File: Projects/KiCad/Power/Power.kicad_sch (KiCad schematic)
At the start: 46 parts, among them J1 Conn_01x02_Pin, J2 Conn_01x02_Pin, J3 Conn_01x02_Pin, J4 Conn_01x02_Pin, Q1 TJ8S06M3L, Q2 TJ8S06M3L, Q3 TJ8S06M3L, SW2 SW_SPDT, U1 NJM7812SDL1, U2 NJM7812SDL1, U3 NJM7812SDL1, U4 LTC4416EMS#PBF

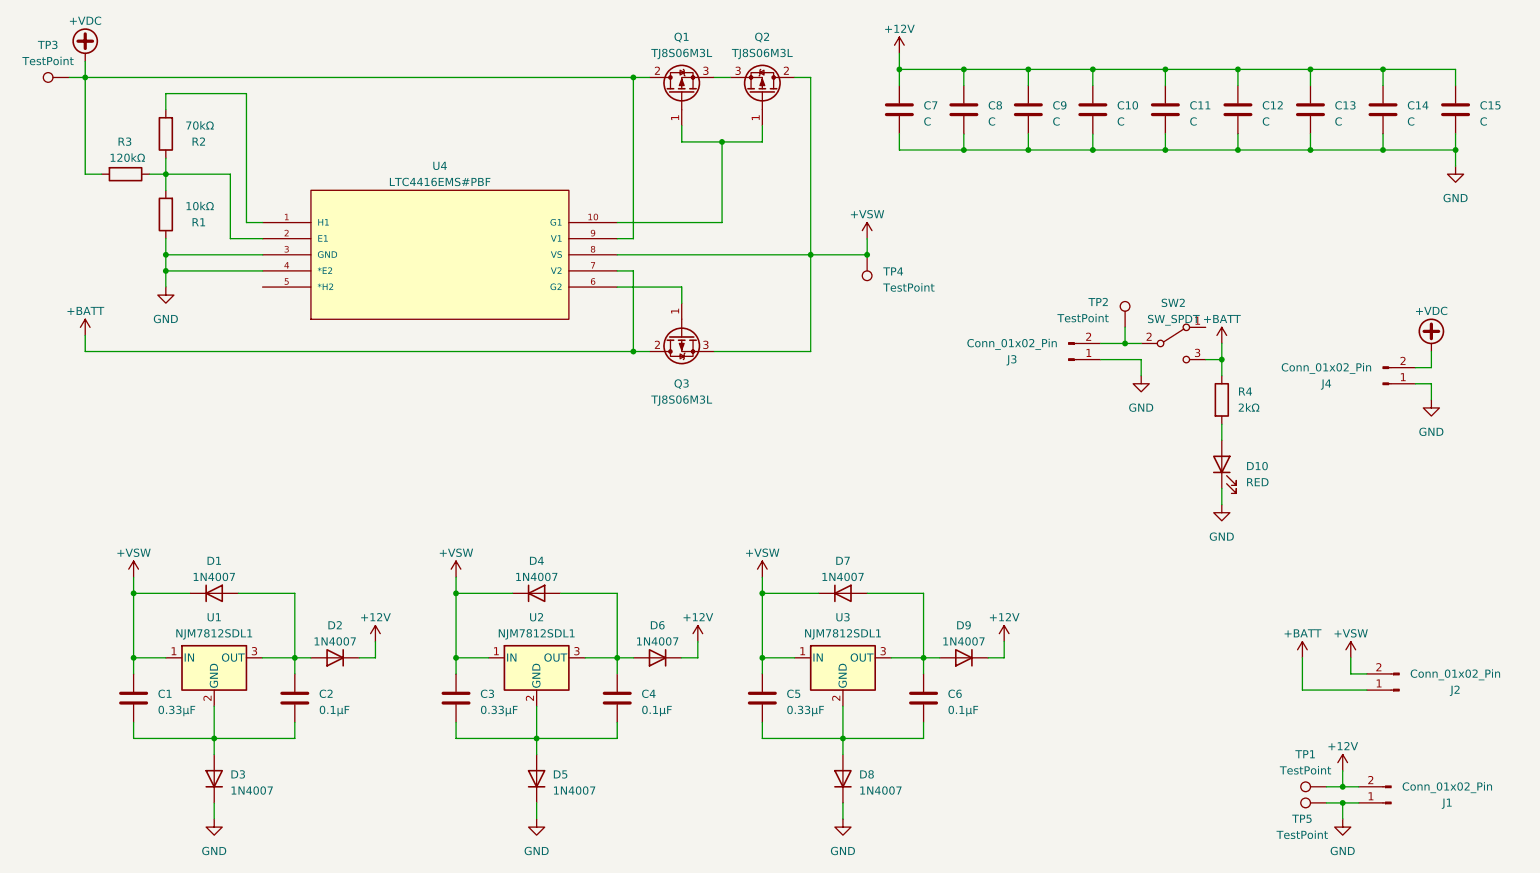
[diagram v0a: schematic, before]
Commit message: STEPファイルを再生成
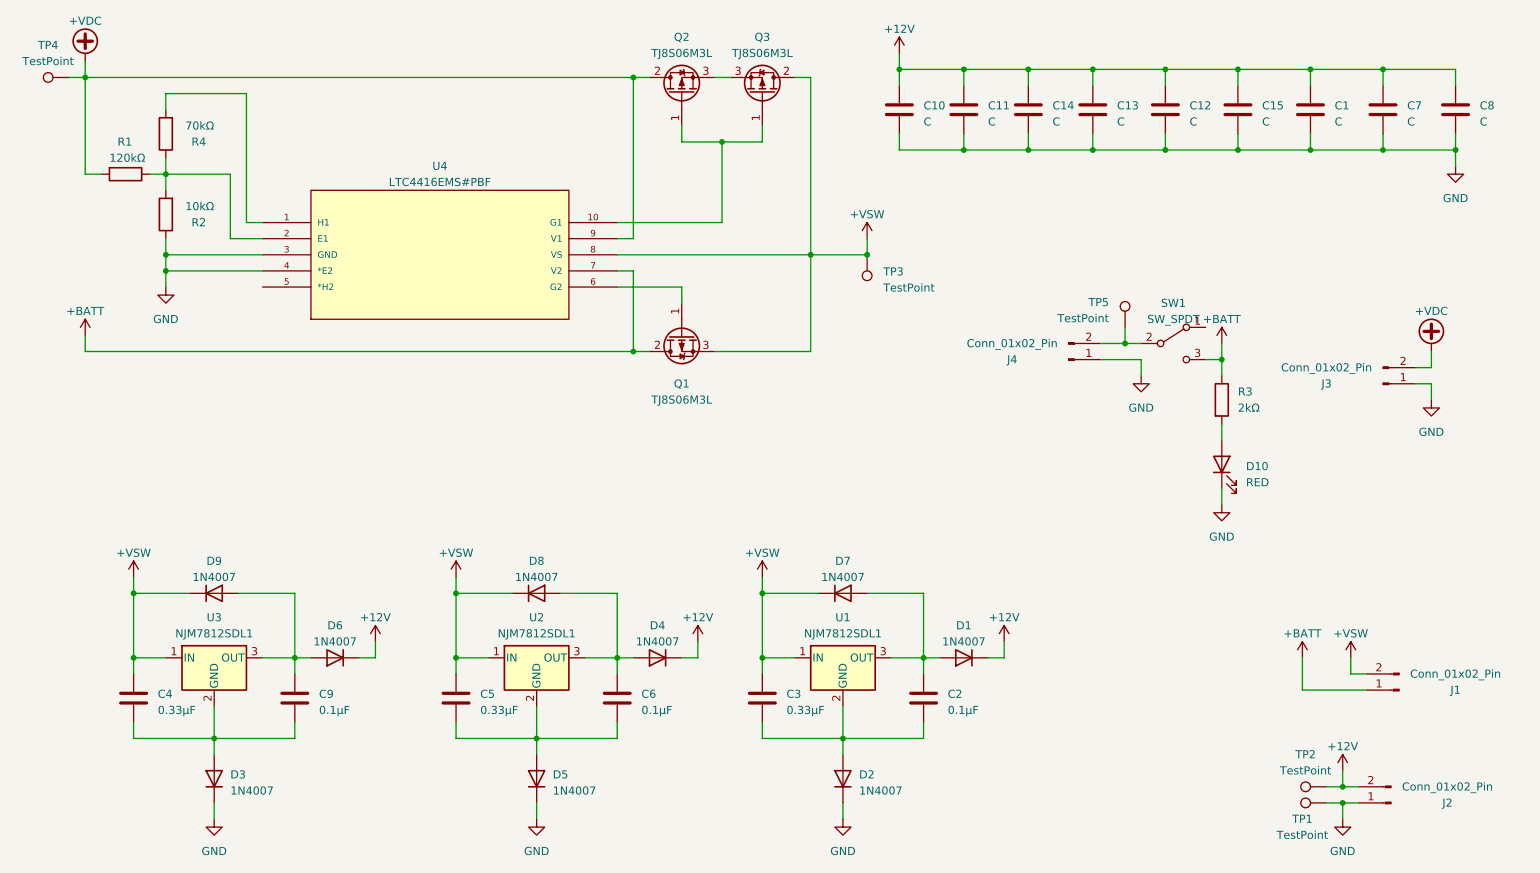
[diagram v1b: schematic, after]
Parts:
- renumbered C13 to C1, C7 to C10, C8 to C11, C11 to C12, C10 to C13, C9 to C14, C12 to C15, C6 to C2, C5 to C3, C1 to C4, C3 to C5, C4 to C6, C14 to C7, C15 to C8, C2 to C9, D9 to D1, D8 to D2, D6 to D4, D2 to D6, D4 to D8, D1 to D9, J2 to J1, J1 to J2, J4 to J3, J3 to J4, Q3 to Q1, Q1 to Q2, Q2 to Q3, R3 to R1, R1 to R2, R4 to R3, R2 to R4, SW2 to SW1, TP5 to TP1, TP1 to TP2, TP4 to TP3, TP3 to TP4, TP2 to TP5, U3 to U1, U1 to U3

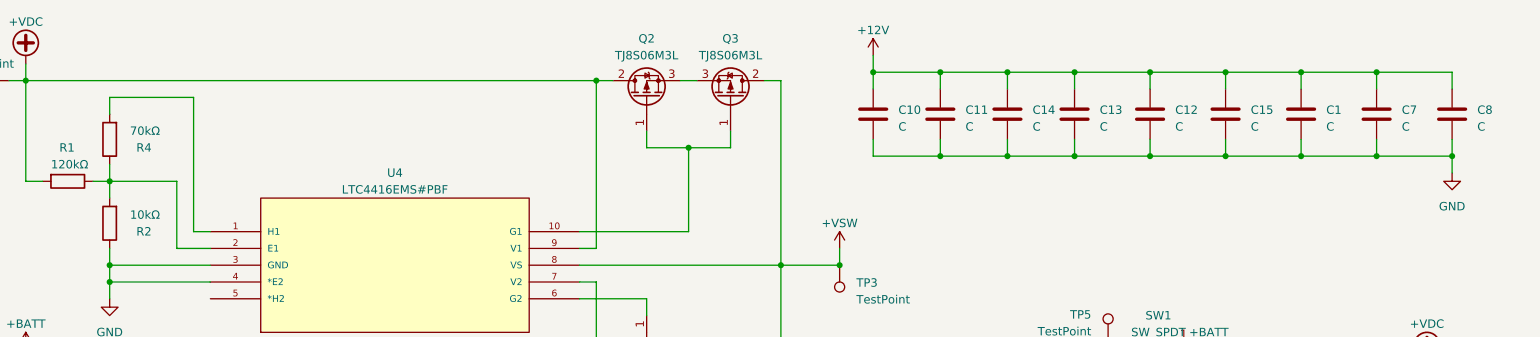
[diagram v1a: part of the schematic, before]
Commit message: 変圧基板の値を修正
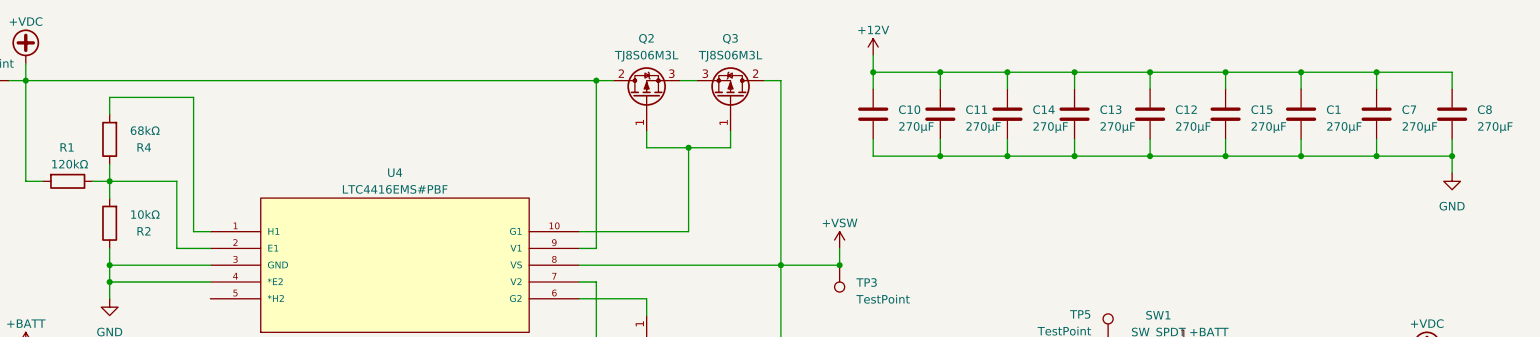
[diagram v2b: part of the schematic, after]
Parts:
- C1, C10, C11, C12, C13, C14, C15, C7, C8: value C -> 270μF
- R4: value 70kΩ -> 68kΩ
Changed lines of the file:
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@@
       (effects (font (size 1.27 1.27)) (justify left))
     )
-    (property "Value" "C" (at 203.2 41.275 0)
+    (property "Value" "270μF" (at 203.2 41.275 0)
       (effects (font (size 1.27 1.27)) (justify left))
     )
@@
       (effects (font (size 1.27 1.27)) (justify left))
     )
-    (property "Value" "C" (at 182.88 41.275 0)
+    (property "Value" "270μF" (at 182.88 41.275 0)
       (effects (font (size 1.27 1.27)) (justify left))
     )
@@
       (effects (font (size 1.27 1.27)) (justify left))
     )
-    (property "Value" "C" (at 214.63 41.275 0)
+    (property "Value" "270μF" (at 214.63 41.275 0)
       (effects (font (size 1.27 1.27)) (justify left))
     )
@@
       (effects (font (size 1.27 1.27)) (justify left))
     )
-    (property "Value" "C" (at 172.72 41.275 0)
+    (property "Value" "270μF" (at 172.72 41.275 0)
       (effects (font (size 1.27 1.27)) (justify left))
     )
@@
       (effects (font (size 1.27 1.27)) (justify left))
     )
-    (property "Value" "C" (at 226.06 41.275 0)
+    (property "Value" "270μF" (at 226.06 41.275 0)
       (effects (font (size 1.27 1.27)) (justify left))
     )
@@
       (effects (font (size 1.27 1.27)) (justify left))
     )
-    (property "Value" "C" (at 260.35 41.275 0)
+    (property "Value" "270μF" (at 260.35 41.275 0)
       (effects (font (size 1.27 1.27)) (justify left))
     )
@@
       (effects (font (size 1.27 1.27)) (justify left))
     )
-    (property "Value" "C" (at 193.04 41.275 0)
+    (property "Value" "270μF" (at 193.04 41.275 0)
       (effects (font (size 1.27 1.27)) (justify left))
     )
@@
       (effects (font (size 1.27 1.27)) (justify left))
     )
-    (property "Value" "C" (at 248.92 41.275 0)
+    (property "Value" "270μF" (at 248.92 41.275 0)
       (effects (font (size 1.27 1.27)) (justify left))
     )
@@
       (effects (font (size 1.27 1.27)) (justify left))
     )
-    (property "Value" "C" (at 237.49 41.275 0)
+    (property "Value" "270μF" (at 237.49 41.275 0)
       (effects (font (size 1.27 1.27)) (justify left))
     )
@@
       (effects (font (size 1.27 1.27)) (justify left))
     )
-    (property "Value" "70kΩ" (at 60.96 41.91 0)
-      (effects (font (size 1.27 1.27)) (justify left))
-    )
+    (property "Value" "68kΩ" (at 60.96 41.91 0)
+      (effects (font (size 1.27 1.27)) (justify left))
+    )
